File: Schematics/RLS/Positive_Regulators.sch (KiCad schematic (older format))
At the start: 25 parts, among them U10 LT1963, U11 LT1963, U8 AD5293, U9 AD5293

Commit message: Lots of changes
Completed Schematic
1/3 Done PCB
Multisim file for testing ADC protection and buffer circuit
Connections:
- net +15V: now also U10.2 (IN); no longer U10.4 (OUT)
- net +V2: now also U10.4 (OUT); no longer U10.2 (IN)
- net +V2_SHDN: now also U10.1 (~SHDN); no longer U10.5 (ADJ)
- net +V1_ADJ: now reaches R23.1, U11.5 (ADJ), U9.4 (RW)
- net +V2_ADJ: now reaches R24.1, U8.4 (RW)
- net +V2_ADJ: now also U10.5 (ADJ); no longer U10.1 (~SHDN)
- net +SDO_SDI: now reaches R22.1, U8.13 (SDO), U9.10 (SDI)
- net +V2_EX_C: now reaches C34.1, U8.7 (EXT_CAP)
- net +V1_EX_C: now reaches C33.1, U9.7 (EXT_CAP)
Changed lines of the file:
@@
 LIBS:valves
 LIBS:arduino_shield
-LIBS:arduino_shieldsNCL
+LIBS:RA30421051
+LIBS:RB496EATR
+LIBS:Daughterboard_Connector
 LIBS:RLS-cache
 EELAYER 25 0
@@
 L LT1963 U10
 U 1 1 59530279
-P 5100 4850
+P 5200 4850
 AR Path="/5952FCB2/59530279" Ref="U10"  Part="1"
 AR Path="/59595696/59530279" Ref="U10"  Part="1"
-F 0 "U10" H 5150 5350 60  0000 C CNN
-F 1 "LT1963" H 5150 5450 60  0000 C CNN
-F 2 "TO_SOT_Packages_THT:TO-220-5_Pentawatt_Multiwatt-5_Vertical_StaggeredType1" H 5150 5350 60  0001 C CNN
-F 3 "" H 5150 5350 60  0001 C CNN
-	1    5100 4850
-	1    0    0    -1
+F 0 "U10" H 5250 5350 60  0000 C CNN
+F 1 "LT1963" H 5250 5450 60  0000 C CNN
+F 2 "TO_SOT_Packages_THT:TO-220-5_Pentawatt_Multiwatt-5_Vertical_StaggeredType1" H 5250 5350 60  0001 C CNN
+F 3 "" H 5250 5350 60  0001 C CNN
+	1    5200 4850
+	-1   0    0    -1
 $EndComp
 $Comp
@@
 Wire Wire Line
 	3000 3250 2950 3250
+Text Label 4650 5300 0    40   ~ 0
++V2_ADJ
+Text Label 4650 2650 0    40   ~ 0
++V1_ADJ
+Text Label 2350 3000 2    40   ~ 0
++V1_EX_C
+Text Label 2350 5650 2    40   ~ 0
++V2_EX_C
+Text Label 2000 4200 1    40   ~ 0
++SDO_SDI
 $EndSCHEMATC

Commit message: Continued PCB and Final Schematic
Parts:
- C22, C24, C26, C28, C30, C32: footprint Capacitors_SMD:C_0603_HandSoldering -> Capacitors_SMD:C_1206_HandSoldering
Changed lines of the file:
@@
 F 0 "C22" H 3475 4750 50  0000 L CNN
 F 1 "0.1uF" H 3475 4550 50  0000 L CNN
-F 2 "Capacitors_SMD:C_0603_HandSoldering" H 3488 4500 50  0001 C CNN
+F 2 "Capacitors_SMD:C_1206_HandSoldering" H 3488 4500 50  0001 C CNN
 F 3 "" H 3450 4650 50  0001 C CNN
 	1    3450 4650
@@
 F 0 "C26" H 2775 4750 50  0000 L CNN
 F 1 "0.1uF" H 2775 4550 50  0000 L CNN
-F 2 "Capacitors_SMD:C_0603_HandSoldering" H 2788 4500 50  0001 C CNN
+F 2 "Capacitors_SMD:C_1206_HandSoldering" H 2788 4500 50  0001 C CNN
 F 3 "" H 2750 4650 50  0001 C CNN
 	1    2750 4650
@@
 F 0 "C28" H 3475 2050 50  0000 L CNN
 F 1 "0.1uF" H 3475 1850 50  0000 L CNN
-F 2 "Capacitors_SMD:C_0603_HandSoldering" H 3488 1800 50  0001 C CNN
+F 2 "Capacitors_SMD:C_1206_HandSoldering" H 3488 1800 50  0001 C CNN
 F 3 "" H 3450 1950 50  0001 C CNN
 	1    3450 1950
@@
 F 0 "C32" H 2775 2050 50  0000 L CNN
 F 1 "0.1uF" H 2775 1850 50  0000 L CNN
-F 2 "Capacitors_SMD:C_0603_HandSoldering" H 2788 1800 50  0001 C CNN
+F 2 "Capacitors_SMD:C_1206_HandSoldering" H 2788 1800 50  0001 C CNN
 F 3 "" H 2750 1950 50  0001 C CNN
 	1    2750 1950
@@
 F 0 "C30" H 3475 3400 50  0000 L CNN
 F 1 "0.1uF" H 3450 3200 50  0000 L CNN
-F 2 "Capacitors_SMD:C_0603_HandSoldering" H 3488 3150 50  0001 C CNN
+F 2 "Capacitors_SMD:C_1206_HandSoldering" H 3488 3150 50  0001 C CNN
 F 3 "" H 3450 3300 50  0001 C CNN
 	1    3450 3300
@@
 F 0 "C24" H 3475 6100 50  0000 L CNN
 F 1 "0.1uF" H 3450 5900 50  0000 L CNN
-F 2 "Capacitors_SMD:C_0603_HandSoldering" H 3488 5850 50  0001 C CNN
+F 2 "Capacitors_SMD:C_1206_HandSoldering" H 3488 5850 50  0001 C CNN
 F 3 "" H 3450 6000 50  0001 C CNN
 	1    3450 6000

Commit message: PCB Layout 90% Done
All that is remaining is the LA traces (moved them and forgot to re-do them) and the SPI and SHDN lines for the digital pots and regs.
Also, do not merge this branch if you can. Have it fully replace the previous folder. There were obsolete files that I removed that Github keeps because it's dumb.
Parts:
- U10, U11: footprint TO_SOT_Packages_THT:TO-220-5_Pentawatt_Multiwatt-5_Vertical_StaggeredType1 -> RLS_CustomFootprints:TO-220-5_Vertical_Type1_w_Heatsink
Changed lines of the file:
@@
 EESchema Schematic File Version 2
-LIBS:RLS-rescue
 LIBS:power
 LIBS:device
@@
 LIBS:contrib
 LIBS:valves
-LIBS:arduino_shield
 LIBS:RA30421051
 LIBS:RB496EATR
@@
 F 0 "U11" H 5250 2700 60  0000 C CNN
 F 1 "LT1963" H 5250 2800 60  0000 C CNN
-F 2 "TO_SOT_Packages_THT:TO-220-5_Pentawatt_Multiwatt-5_Vertical_StaggeredType1" H 5250 2700 60  0001 C CNN
+F 2 "RLS_CustomFootprints:TO-220-5_Vertical_Type1_w_Heatsink" H 5250 2700 60  0001 C CNN
 F 3 "" H 5250 2700 60  0001 C CNN
 	1    5200 2200
@@
 F 0 "U10" H 5250 5350 60  0000 C CNN
 F 1 "LT1963" H 5250 5450 60  0000 C CNN
-F 2 "TO_SOT_Packages_THT:TO-220-5_Pentawatt_Multiwatt-5_Vertical_StaggeredType1" H 5250 5350 60  0001 C CNN
+F 2 "RLS_CustomFootprints:TO-220-5_Vertical_Type1_w_Heatsink" H 5250 5350 60  0001 C CNN
 F 3 "" H 5250 5350 60  0001 C CNN
 	1    5200 4850
@@
 	3300 4350 3200 4350
 Wire Wire Line
-	3300 4650 3200 4650
+	3200 4650 3300 4650
 Connection ~ 3200 4650
 Text GLabel 3200 4250 1    60   Input ~ 0
@@
 $EndComp
 Wire Wire Line
-	4900 2950 4900 2850
+	4900 2850 4900 2950
 Connection ~ 4900 2850
 Wire Wire Line
@@
 $EndComp
 Wire Wire Line
-	4900 5600 4900 5500
+	4900 5500 4900 5600
 Connection ~ 4900 5500
 Wire Wire Line

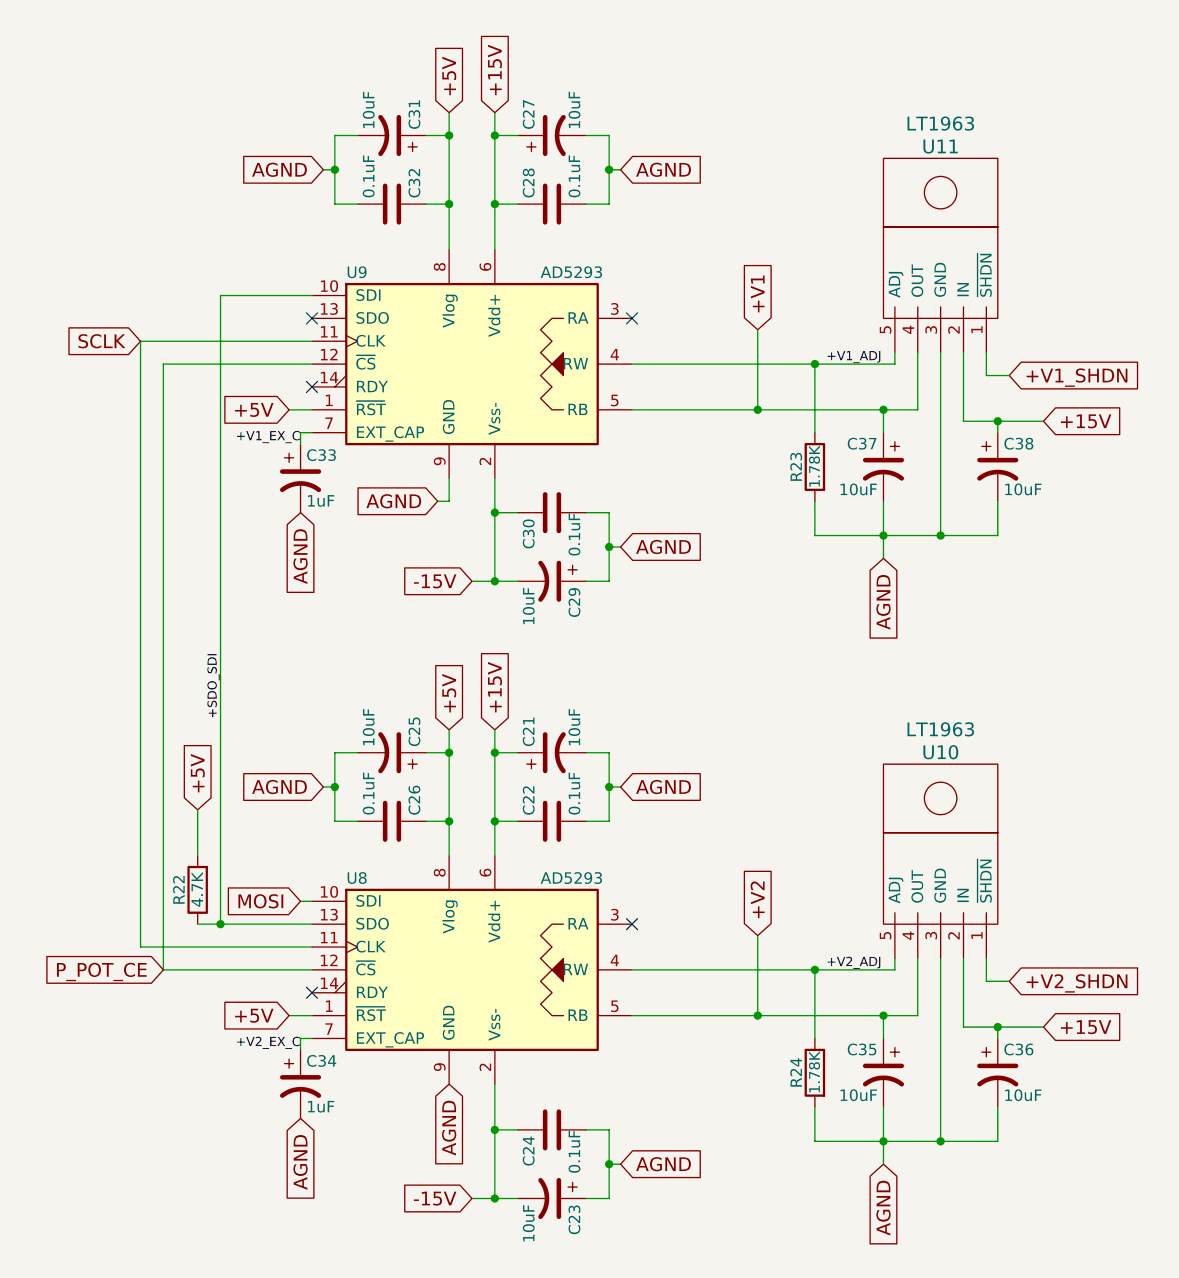
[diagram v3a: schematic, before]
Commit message: Finished PCB but...
Somehow managed to break the schematic file. I know how to fix it, but it is tedious and pointless for now (one has to go through every single individual component and verify that it is the same in the PCB, since the annotation script fucked everything up in the schematic, and therefore any new Netlist).
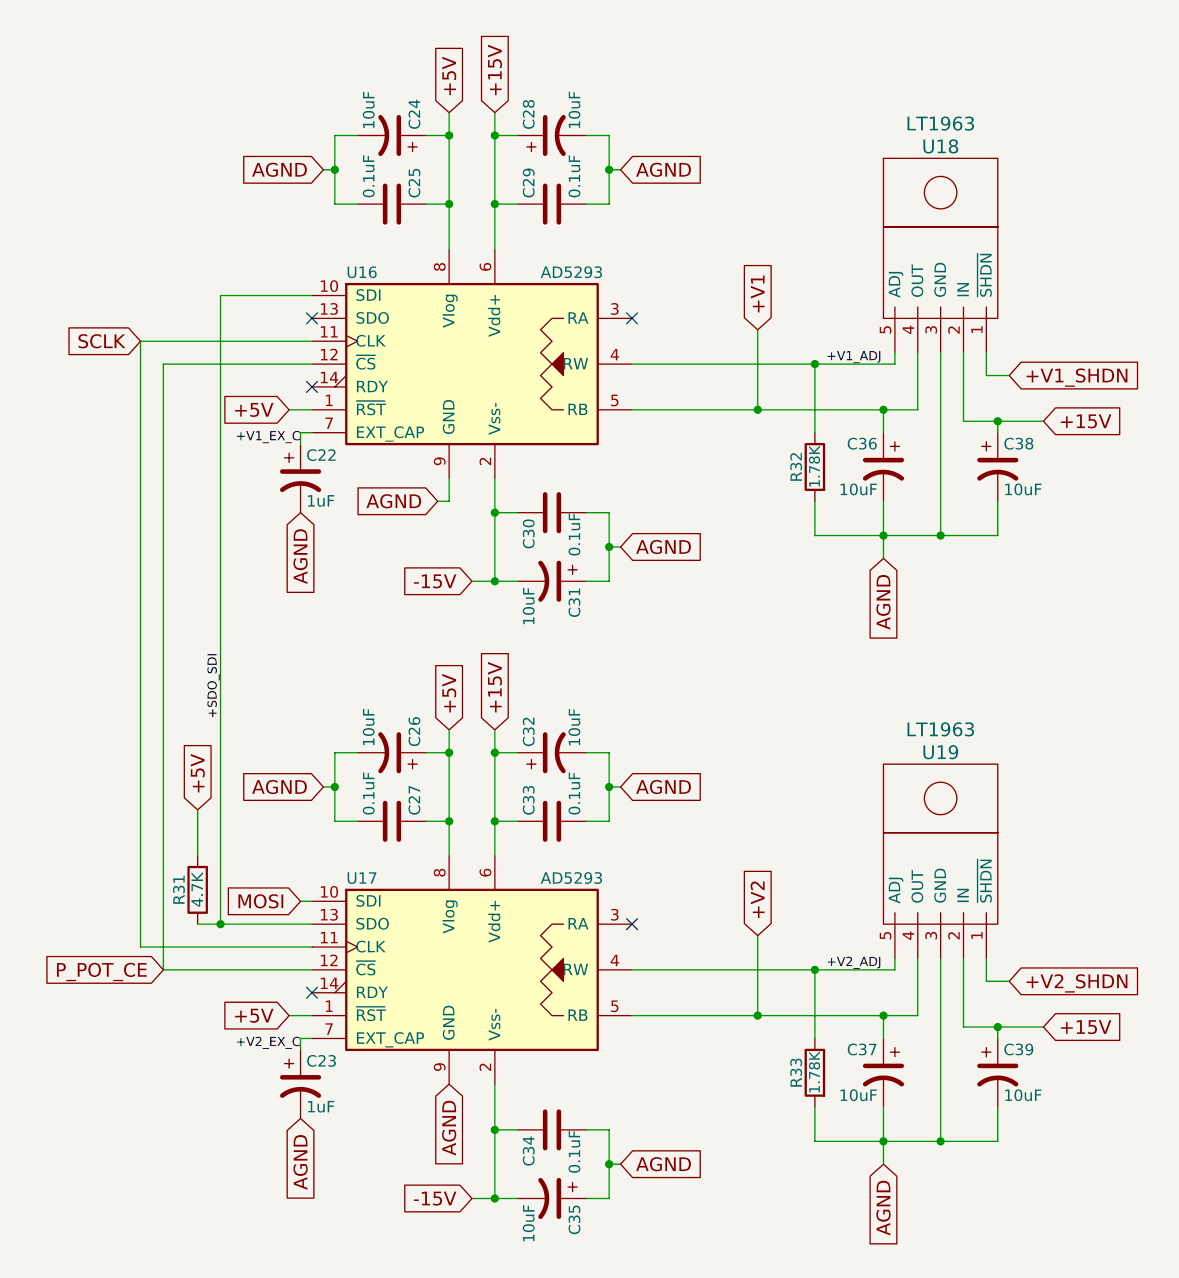
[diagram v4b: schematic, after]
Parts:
- renumbered C33 to C22, C34 to C23, C31 to C24, C32 to C25, C25 to C26, C26 to C27, C27 to C28, C28 to C29, C29 to C31, C21 to C32, C22 to C33, C24 to C34, C23 to C35, C37 to C36, C35 to C37, C36 to C39, R22 to R31, R23 to R32, R24 to R33, U9 to U16, U8 to U17, U11 to U18, U10 to U19
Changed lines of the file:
@@
 $EndDescr
 $Comp
-L LT1963 U11
+L LT1963 U18
 U 1 1 5953022A
 P 5200 2200
-AR Path="/5952FCB2/5953022A" Ref="U11"  Part="1"
-AR Path="/59595696/5953022A" Ref="U11"  Part="1"
-F 0 "U11" H 5250 2700 60  0000 C CNN
+F 0 "U18" H 5250 2700 60  0000 C CNN
 F 1 "LT1963" H 5250 2800 60  0000 C CNN
 F 2 "RLS_CustomFootprints:TO-220-5_Vertical_Type1_w_Heatsink" H 5250 2700 60  0001 C CNN
@@
 $EndComp
 $Comp
-L LT1963 U10
+L LT1963 U19
 U 1 1 59530279
 P 5200 4850
-AR Path="/5952FCB2/59530279" Ref="U10"  Part="1"
-AR Path="/59595696/59530279" Ref="U10"  Part="1"
-F 0 "U10" H 5250 5350 60  0000 C CNN
+F 0 "U19" H 5250 5350 60  0000 C CNN
 F 1 "LT1963" H 5250 5450 60  0000 C CNN
 F 2 "RLS_CustomFootprints:TO-220-5_Vertical_Type1_w_Heatsink" H 5250 5350 60  0001 C CNN
@@
 $EndComp
 $Comp
-L AD5293-RESCUE-RLS U8
+L AD5293-RESCUE-RLS U17
 U 1 1 595A3981
 P 3100 5300
-AR Path="/5952FCB2/595A3981" Ref="U8"  Part="1"
-AR Path="/59595696/595A3981" Ref="U8"  Part="1"
-F 0 "U8" H 2550 5700 50  0000 L CNN
+F 0 "U17" H 2550 5700 50  0000 L CNN
 F 1 "AD5293" H 3400 5700 50  0000 L CNN
 F 2 "SMD_Packages:SSOP-14" H 3100 5300 50  0001 C CNN
@@
 $EndComp
 $Comp
-L AD5293-RESCUE-RLS U9
+L AD5293-RESCUE-RLS U16
 U 1 1 595A3988
 P 3100 2650
-AR Path="/5952FCB2/595A3988" Ref="U9"  Part="1"
-AR Path="/59595696/595A3988" Ref="U9"  Part="1"
-F 0 "U9" H 2550 3050 50  0000 L CNN
+F 0 "U16" H 2550 3050 50  0000 L CNN
 F 1 "AD5293" H 3400 3050 50  0000 L CNN
 F 2 "SMD_Packages:SSOP-14" H 3100 2650 50  0001 C CNN
@@
 $EndComp
 $Comp
-L CP1 C33
+L CP1 C22
 U 1 1 595A398F
 P 2350 3150
-AR Path="/5952FCB2/595A398F" Ref="C33"  Part="1"
-AR Path="/59595696/595A398F" Ref="C33"  Part="1"
-F 0 "C33" H 2375 3250 50  0000 L CNN
+F 0 "C22" H 2375 3250 50  0000 L CNN
 F 1 "1uF" H 2375 3050 50  0000 L CNN
 F 2 "Capacitors_SMD:CP_Elec_4x5.3" H 2350 3150 50  0001 C CNN
@@
 $EndComp
 $Comp
-L CP1 C34
+L CP1 C23
 U 1 1 595A3996
 P 2350 5800
-AR Path="/5952FCB2/595A3996" Ref="C34"  Part="1"
-AR Path="/59595696/595A3996" Ref="C34"  Part="1"
-F 0 "C34" H 2375 5900 50  0000 L CNN
+F 0 "C23" H 2375 5900 50  0000 L CNN
 F 1 "1uF" H 2375 5700 50  0000 L CNN
 F 2 "Capacitors_SMD:CP_Elec_4x5.3" H 2350 5800 50  0001 C CNN
@@
 $EndComp
 $Comp
-L CP1 C21
+L CP1 C32
 U 1 1 595A399D
 P 3450 4350
-AR Path="/5952FCB2/595A399D" Ref="C21"  Part="1"
-AR Path="/59595696/595A399D" Ref="C21"  Part="1"
-F 0 "C21" H 3475 4450 50  0000 L CNN
+F 0 "C32" H 3475 4450 50  0000 L CNN
 F 1 "10uF" H 3475 4250 50  0000 L CNN
 F 2 "Capacitors_SMD:CP_Elec_4x5.3" H 3450 4350 50  0001 C CNN
@@
 $EndComp
 $Comp
-L C C22
+L C C33
 U 1 1 595A39A4
 P 3450 4650
-AR Path="/5952FCB2/595A39A4" Ref="C22"  Part="1"
-AR Path="/59595696/595A39A4" Ref="C22"  Part="1"
-F 0 "C22" H 3475 4750 50  0000 L CNN
+F 0 "C33" H 3475 4750 50  0000 L CNN
 F 1 "0.1uF" H 3475 4550 50  0000 L CNN
 F 2 "Capacitors_SMD:C_1206_HandSoldering" H 3488 4500 50  0001 C CNN
@@
 $EndComp
 $Comp
-L R R22
+L R R31
 U 1 1 595A39AB
 P 1900 4950
-AR Path="/5952FCB2/595A39AB" Ref="R22"  Part="1"
-AR Path="/59595696/595A39AB" Ref="R22"  Part="1"
-F 0 "R22" V 1980 4950 50  0000 C CNN
+F 0 "R31" V 1980 4950 50  0000 C CNN
 F 1 "4.7K" V 1900 4950 50  0000 C CNN
 F 2 "Resistors_SMD:R_0805_HandSoldering" V 1830 4950 50  0001 C CNN
@@
 	2350 2950 2350 3000
 $Comp
-L CP1 C25
+L CP1 C26
 U 1 1 595A39B6
 P 2750 4350
-AR Path="/5952FCB2/595A39B6" Ref="C25"  Part="1"
-AR Path="/59595696/595A39B6" Ref="C25"  Part="1"
-F 0 "C25" H 2775 4450 50  0000 L CNN
+F 0 "C26" H 2775 4450 50  0000 L CNN
 F 1 "10uF" H 2775 4250 50  0000 L CNN
 F 2 "Capacitors_SMD:CP_Elec_4x5.3" H 2750 4350 50  0001 C CNN
@@
 $EndComp
 $Comp
-L C C26
+L C C27
 U 1 1 595A39BD
 P 2750 4650
-AR Path="/5952FCB2/595A39BD" Ref="C26"  Part="1"
-AR Path="/59595696/595A39BD" Ref="C26"  Part="1"
-F 0 "C26" H 2775 4750 50  0000 L CNN
+F 0 "C27" H 2775 4750 50  0000 L CNN
 F 1 "0.1uF" H 2775 4550 50  0000 L CNN
 F 2 "Capacitors_SMD:C_1206_HandSoldering" H 2788 4500 50  0001 C CNN
@@
 Connection ~ 3200 4350
 $Comp
-L CP1 C27
+L CP1 C28
 U 1 1 595A39DC
 P 3450 1650
-AR Path="/5952FCB2/595A39DC" Ref="C27"  Part="1"
-AR Path="/59595696/595A39DC" Ref="C27"  Part="1"
-F 0 "C27" H 3475 1750 50  0000 L CNN
+F 0 "C28" H 3475 1750 50  0000 L CNN
 F 1 "10uF" H 3475 1550 50  0000 L CNN
 F 2 "Capacitors_SMD:CP_Elec_4x5.3" H 3450 1650 50  0001 C CNN
@@
 $EndComp
 $Comp
-L C C28
+L C C29
 U 1 1 595A39E3
 P 3450 1950
-AR Path="/5952FCB2/595A39E3" Ref="C28"  Part="1"
-AR Path="/59595696/595A39E3" Ref="C28"  Part="1"
-F 0 "C28" H 3475 2050 50  0000 L CNN
+F 0 "C29" H 3475 2050 50  0000 L CNN
 F 1 "0.1uF" H 3475 1850 50  0000 L CNN
 F 2 "Capacitors_SMD:C_1206_HandSoldering" H 3488 1800 50  0001 C CNN
@@
 $EndComp
 $Comp
-L C C32
+L C C25
 U 1 1 595A39F1
 P 2750 1950
-AR Path="/5952FCB2/595A39F1" Ref="C32"  Part="1"
-AR Path="/59595696/595A39F1" Ref="C32"  Part="1"
-F 0 "C32" H 2775 2050 50  0000 L CNN
+F 0 "C25" H 2775 2050 50  0000 L CNN
 F 1 "0.1uF" H 2775 1850 50  0000 L CNN
 F 2 "Capacitors_SMD:C_1206_HandSoldering" H 2788 1800 50  0001 C CNN
@@
 AGND
 $Comp
-L CP1 C29
+L CP1 C31
 U 1 1 595A3A12
 P 3450 3600
-AR Path="/5952FCB2/595A3A12" Ref="C29"  Part="1"
-AR Path="/59595696/595A3A12" Ref="C29"  Part="1"
-F 0 "C29" H 3475 3700 50  0000 L CNN
+F 0 "C31" H 3475 3700 50  0000 L CNN
 F 1 "10uF" H 3475 3500 50  0000 L CNN
 F 2 "Capacitors_SMD:CP_Elec_4x5.3" H 3450 3600 50  0001 C CNN
@@
 U 1 1 595A3A19
 P 3450 3300
-AR Path="/5952FCB2/595A3A19" Ref="C30"  Part="1"
-AR Path="/59595696/595A3A19" Ref="C30"  Part="1"
 F 0 "C30" H 3475 3400 50  0000 L CNN
 F 1 "0.1uF" H 3450 3200 50  0000 L CNN
@@
 -15V
 $Comp
-L CP1 C23
+L CP1 C35
 U 1 1 595A3A2C
 P 3450 6300
-AR Path="/5952FCB2/595A3A2C" Ref="C23"  Part="1"
-AR Path="/59595696/595A3A2C" Ref="C23"  Part="1"
-F 0 "C23" H 3475 6400 50  0000 L CNN
+F 0 "C35" H 3475 6400 50  0000 L CNN
 F 1 "10uF" H 3475 6200 50  0000 L CNN
 F 2 "Capacitors_SMD:CP_Elec_4x5.3" H 3450 6300 50  0001 C CNN
@@
 $EndComp
 $Comp
-L C C24
+L C C34
 U 1 1 595A3A33
 P 3450 6000
-AR Path="/5952FCB2/595A3A33" Ref="C24"  Part="1"
-AR Path="/59595696/595A3A33" Ref="C24"  Part="1"
-F 0 "C24" H 3475 6100 50  0000 L CNN
+F 0 "C34" H 3475 6100 50  0000 L CNN
 F 1 "0.1uF" H 3450 5900 50  0000 L CNN
 F 2 "Capacitors_SMD:C_1206_HandSoldering" H 3488 5850 50  0001 C CNN
@@
 AGND
 $Comp
-L CP1 C31
+L CP1 C24
 U 1 1 595A39EA
 P 2750 1650
-AR Path="/5952FCB2/595A39EA" Ref="C31"  Part="1"
-AR Path="/59595696/595A39EA" Ref="C31"  Part="1"
-F 0 "C31" H 2775 1750 50  0000 L CNN
+F 0 "C24" H 2775 1750 50  0000 L CNN
 F 1 "10uF" H 2775 1550 50  0000 L CNN
 F 2 "Capacitors_SMD:CP_Elec_4x5.3" H 2750 1650 50  0001 C CNN
@@
 	5050 2850 5050 2600
 $Comp
-L R R23
+L R R32
 U 1 1 595A712D
 P 4600 3100
-AR Path="/5952FCB2/595A712D" Ref="R23"  Part="1"
-AR Path="/59595696/595A712D" Ref="R23"  Part="1"
-F 0 "R23" V 4680 3100 50  0000 C CNN
+F 0 "R32" V 4680 3100 50  0000 C CNN
 F 1 "1.78K" V 4600 3100 47  0000 C CNN
 F 2 "Resistors_SMD:R_1206_HandSoldering" V 4530 3100 50  0001 C CNN
@@
 $EndComp
 $Comp
-L CP1 C37
+L CP1 C36
 U 1 1 595A7134
 P 4900 3100
-AR Path="/5952FCB2/595A7134" Ref="C37"  Part="1"
-AR Path="/59595696/595A7134" Ref="C37"  Part="1"
-F 0 "C37" H 4925 3200 50  0000 L CNN
+F 0 "C36" H 4925 3200 50  0000 L CNN
 F 1 "10uF" H 4925 3000 50  0000 L CNN
 F 2 "Capacitors_SMD:CP_Elec_4x5.3" H 4900 3100 50  0001 C CNN
@@
 U 1 1 595A713B
 P 5400 3100
-AR Path="/5952FCB2/595A713B" Ref="C38"  Part="1"
-AR Path="/59595696/595A713B" Ref="C38"  Part="1"
 F 0 "C38" H 5425 3200 50  0000 L CNN
 F 1 "10uF" H 5425 3000 50  0000 L CNN
@@
 	5050 5500 5050 5250
 $Comp
-L R R24
+L R R33
 U 1 1 5958D2DA
 P 4600 5750
-AR Path="/5952FCB2/5958D2DA" Ref="R24"  Part="1"
-AR Path="/59595696/5958D2DA" Ref="R24"  Part="1"
-F 0 "R24" V 4680 5750 50  0000 C CNN
+F 0 "R33" V 4680 5750 50  0000 C CNN
 F 1 "1.78K" V 4600 5750 47  0000 C CNN
 F 2 "Resistors_SMD:R_1206_HandSoldering" V 4530 5750 50  0001 C CNN
@@
 $EndComp
 $Comp
-L CP1 C35
+L CP1 C37
 U 1 1 5958D2E1
 P 4900 5750
-AR Path="/5952FCB2/5958D2E1" Ref="C35"  Part="1"
-AR Path="/59595696/5958D2E1" Ref="C35"  Part="1"
-F 0 "C35" H 4925 5850 50  0000 L CNN
+F 0 "C37" H 4925 5850 50  0000 L CNN
 F 1 "10uF" H 4925 5650 50  0000 L CNN
 F 2 "Capacitors_SMD:CP_Elec_4x5.3" H 4900 5750 50  0001 C CNN
@@
 $EndComp
 $Comp
-L CP1 C36
+L CP1 C39
 U 1 1 5958D2E8
 P 5400 5750
-AR Path="/5952FCB2/5958D2E8" Ref="C36"  Part="1"
-AR Path="/59595696/5958D2E8" Ref="C36"  Part="1"
-F 0 "C36" H 5425 5850 50  0000 L CNN
+F 0 "C39" H 5425 5850 50  0000 L CNN
 F 1 "10uF" H 5425 5650 50  0000 L CNN
 F 2 "Capacitors_SMD:CP_Elec_4x5.3" H 5400 5750 50  0001 C CNN

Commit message: MAJOR CHANGE! READ BELOW
Due to layout issues, I changed the pins used for the variable regulator shutdown lines. +V1_SHDN is now AA9, +V2_SHDN is now AA8, -V1_SHDN is now AA11, and -V2_SHDN is now AA10. MAKE SURE TO CHANGE THE RESPECTIVE CODE (Paolo).

Included in this upload is the pre-design review finish PCB and Schematic, with pdf files of each for printing and easy reference.
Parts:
- U16, U17: footprint SMD_Packages:SSOP-14 -> Housings_SSOP:TSSOP-14_4.4x5mm_Pitch0.65mm
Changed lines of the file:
@@
 Sheet 5 7
 Title "Remote Lab System"
-Date ""
-Rev ""
-Comp ""
+Date "2017-07-18"
+Rev "15"
+Comp "University of Washington, Bothell"
 Comment1 ""
 Comment2 ""
@@
 F 0 "U17" H 2550 5700 50  0000 L CNN
 F 1 "AD5293" H 3400 5700 50  0000 L CNN
-F 2 "SMD_Packages:SSOP-14" H 3100 5300 50  0001 C CNN
+F 2 "Housings_SSOP:TSSOP-14_4.4x5mm_Pitch0.65mm" H 3100 5300 50  0001 C CNN
 F 3 "" H 3100 5300 50  0001 C CNN
 	1    3100 5300
@@
 F 0 "U16" H 2550 3050 50  0000 L CNN
 F 1 "AD5293" H 3400 3050 50  0000 L CNN
-F 2 "SMD_Packages:SSOP-14" H 3100 2650 50  0001 C CNN
+F 2 "Housings_SSOP:TSSOP-14_4.4x5mm_Pitch0.65mm" H 3100 2650 50  0001 C CNN
 F 3 "" H 3100 2650 50  0001 C CNN
 	1    3100 2650
